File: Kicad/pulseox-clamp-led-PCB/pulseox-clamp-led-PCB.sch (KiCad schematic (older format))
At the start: 5 parts, among them P1 Header 3

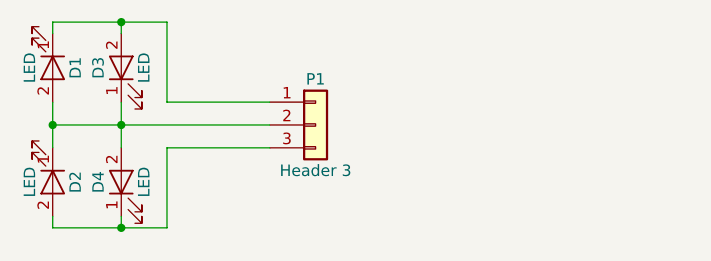
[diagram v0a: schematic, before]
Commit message: Added output PDF files from Kicad project
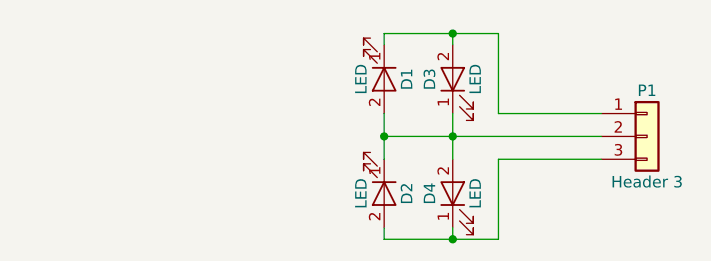
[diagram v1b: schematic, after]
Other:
- moved on the sheet: D1, D2, D3, D4, P1
